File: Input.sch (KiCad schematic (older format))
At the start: 42 parts, among them SW1 Rotary encoder EC11 Plum 15mm, U3 INA826AID, U4 INA826AID, U5 ADS1115IDGS, U6 LM393, U7 74HC125

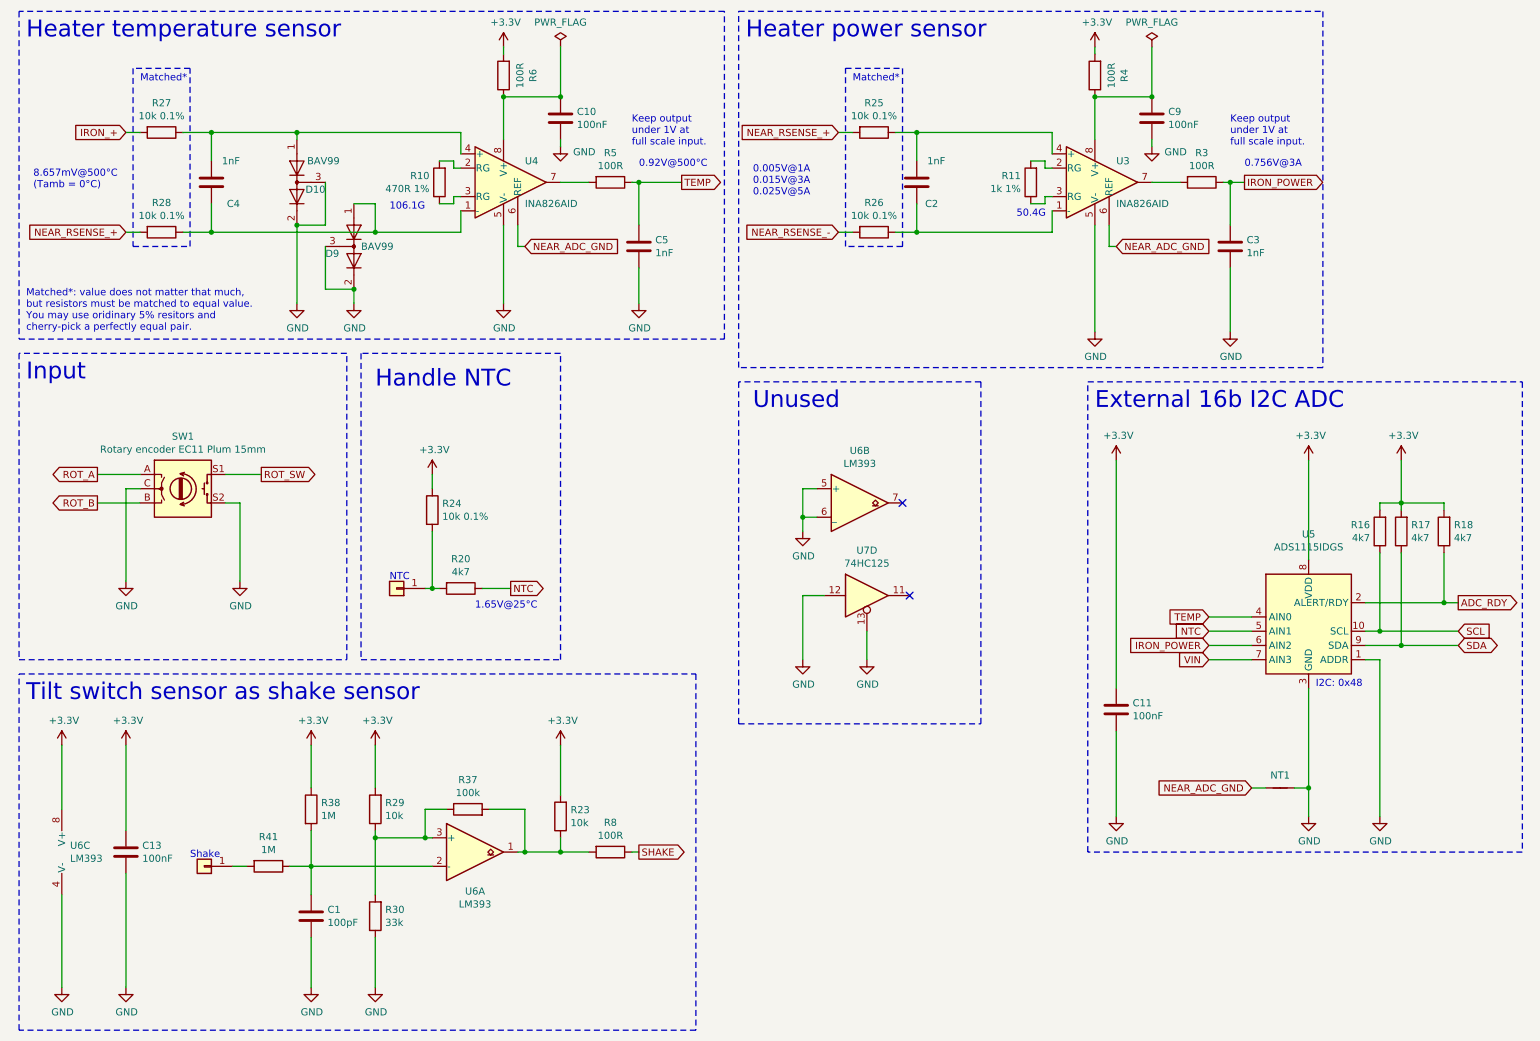
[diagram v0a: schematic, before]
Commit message: Added overheat protection that works, but very noisy.
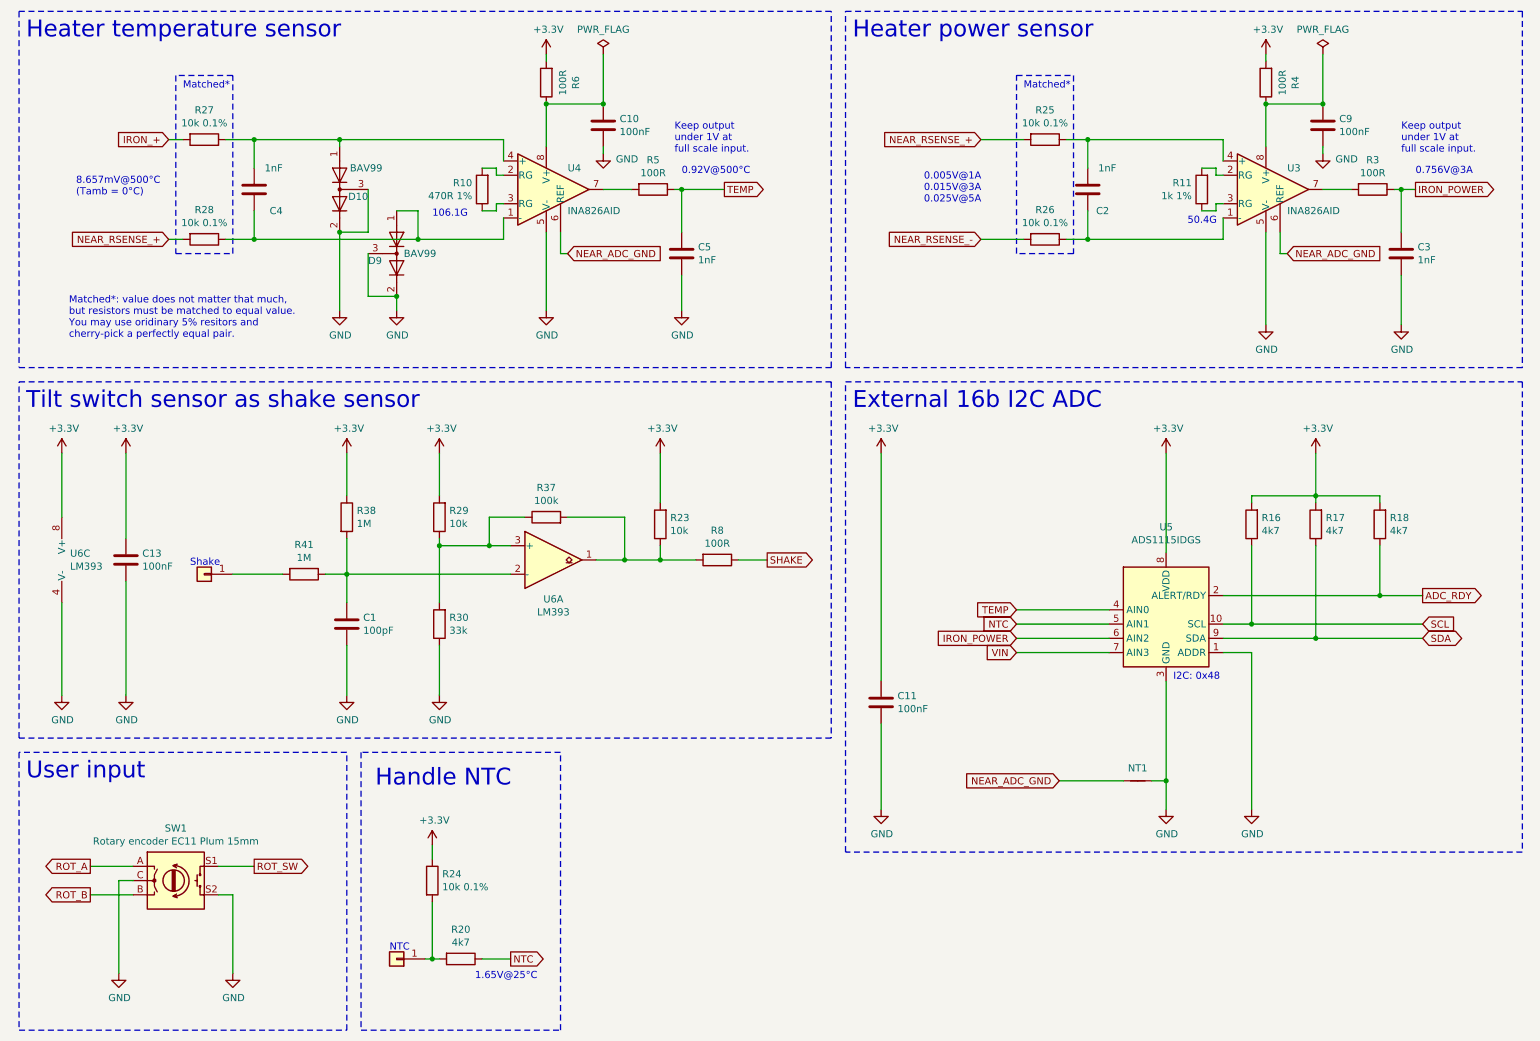
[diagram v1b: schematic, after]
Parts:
- removed unit 2 of U6
- removed U7: 74HC125, Package_SO:SOIC-14_3.9x8.7mm_P1.27mm, symbol 74xx:74LS125
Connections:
- no-connect marks 2 -> 0
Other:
- note added: "User input"
- note removed: "Input"
- note removed: "Unused"
- moved on the sheet: C1, C10, C11, C13, C2, C3, C4, C5, C9, D10, D9, NT1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

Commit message: V2.0 pcb.
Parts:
- removed C1: 100pF, Capacitor_SMD:C_0805_2012Metric_Pad1.18x1.45mm_HandSolder, symbol Device:C
- removed C13, C9: 100nF, Capacitor_SMD:C_0805_2012Metric_Pad1.18x1.45mm_HandSolder, symbol Device:C
- removed C3, C5: 1nF, Capacitor_SMD:C_0805_2012Metric_Pad1.18x1.45mm_HandSolder, symbol Device:C
- removed R16, R17, R20: 4k7, Resistor_SMD:R_0805_2012Metric_Pad1.20x1.40mm_HandSolder, symbol Device:R
- removed R23, R29: 10k, Resistor_SMD:R_0805_2012Metric_Pad1.20x1.40mm_HandSolder, symbol Device:R
- removed R24, R25, R27, R28: 10k 0.1%, Resistor_SMD:R_0805_2012Metric_Pad1.20x1.40mm_HandSolder, symbol Device:R
- removed R3, R4, R5, R6, R8: 100R, Resistor_SMD:R_0805_2012Metric_Pad1.20x1.40mm_HandSolder, symbol Device:R
- removed R37: 100k, Resistor_SMD:R_0805_2012Metric_Pad1.20x1.40mm_HandSolder, symbol Device:R
- removed R41: 1M, Resistor_SMD:R_0805_2012Metric_Pad1.20x1.40mm_HandSolder, symbol Device:R
- removed U3: INA826AID, Package_SO:SOIC-8_3.9x4.9mm_P1.27mm, symbol Amplifier_Instrumentation-extra:INA826
- removed U6: LM393, Package_SO:SO-8_3.9x4.9mm_P1.27mm, symbol Comparator:LM393
- added C30, C31: 100nF, Capacitor_SMD:C_0805_2012Metric_Pad1.18x1.45mm_HandSolder, symbol Device:C
- added R10: 100R, Resistor_SMD:R_0805_2012Metric_Pad1.20x1.40mm_HandSolder, symbol Device:R
- added R51: 4k7, Resistor_SMD:R_0805_2012Metric_Pad1.20x1.40mm_HandSolder, symbol Device:R
- added R60, R61, R62, R64: 10k 0.1%, Resistor_SMD:R_0805_2012Metric_Pad1.20x1.40mm_HandSolder, symbol Device:R
- added R81: 1M, Resistor_SMD:R_0805_2012Metric_Pad1.20x1.40mm_HandSolder, symbol Device:R
- added U4: INA826AID, Package_SO:SOIC-8_3.9x4.9mm_P1.27mm, symbol Amplifier_Instrumentation-extra:INA826
- C10: value 100nF -> 100pF
- R11: value 1k 1% -> 100R
- R30: value 33k -> 1k 1%
- renumbered C4 to C20, C2 to C21, C11 to C32, D10 to D1, D9 to D2, J106 to J1, J105 to J2, R10 to R21, R18 to R50, R26 to R63, R38 to R80, U5 to U2, U4 to U3
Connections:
- net +3V3: now also R11.2, R10.2, R64.1
- net GND: now also C30.2, C31.2, U4.5 (V-); no longer R30.1
- net IRON_+: now also R60.2
- net IRON_POWER: now also U4.7
- net NEAR_ADC_GND: now also U4.6 (REF)
- net NEAR_RSENSE_+: now also R61.2, R62.2
- net NTC: now also R51.1
- net TEMP: now also U3.7
- net at C20.2, D2.1 (K), U3.1 (-): now also R61.1
- net at C20.1, D1.1 (K), U3.4 (+): now also R60.1
- net at U3.8 (V+): now also C30.1, R10.1; no longer C10.1
- net at J2.1 (Pin_1): now also R51.2, R64.2
- net at J1.1 (Pin_1): now also R81.2
- net AIN_COMP: now reaches R80.2
- net AIN_COMP: now also C10.1, R81.1
- net at C21.1: now also R62.1, U4.4 (+)
- net at C21.2, R63.1: now also U4.1 (-)
- net at R11.1: now also C31.1, U4.8 (V+)
- net at R30.2: now also U4.2 (RG)
- net SCL renamed HEAT_SCL
- net SDA renamed HEAT_SDA
- new net: R30.1, U4.3 (RG)
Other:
- moved on the sheet: R80, SW1

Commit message: V2.0 pcb.
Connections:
- net IRON_POWER renamed IRON_CURRENT
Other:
- note added: "Heater current sensor"
- note removed: "Heater power sensor"
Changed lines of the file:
@@
 Sheet 2 5
 Title "IoT12-hardware input and sensors"
-Date "2021-02-21"
+Date "2021-02-22"
 Rev "V2.0"
 Comp ""
@@
 	11100 550  11100 3050
 Text Notes 6400 750  0    118  ~ 0
-Heater power sensor
+Heater current sensor
 Text GLabel 10350 1800 2    50   Output ~ 0
-IRON_POWER
+IRON_CURRENT
 $Comp
 L Device:Rotary_Encoder_Switch SW1
@@
 TEMP
 Text GLabel 7550 4950 0    50   Input ~ 0
-IRON_POWER
+IRON_CURRENT
 Text GLabel 7550 5050 0    50   Input ~ 0
 VIN
